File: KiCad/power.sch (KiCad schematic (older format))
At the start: 16 parts

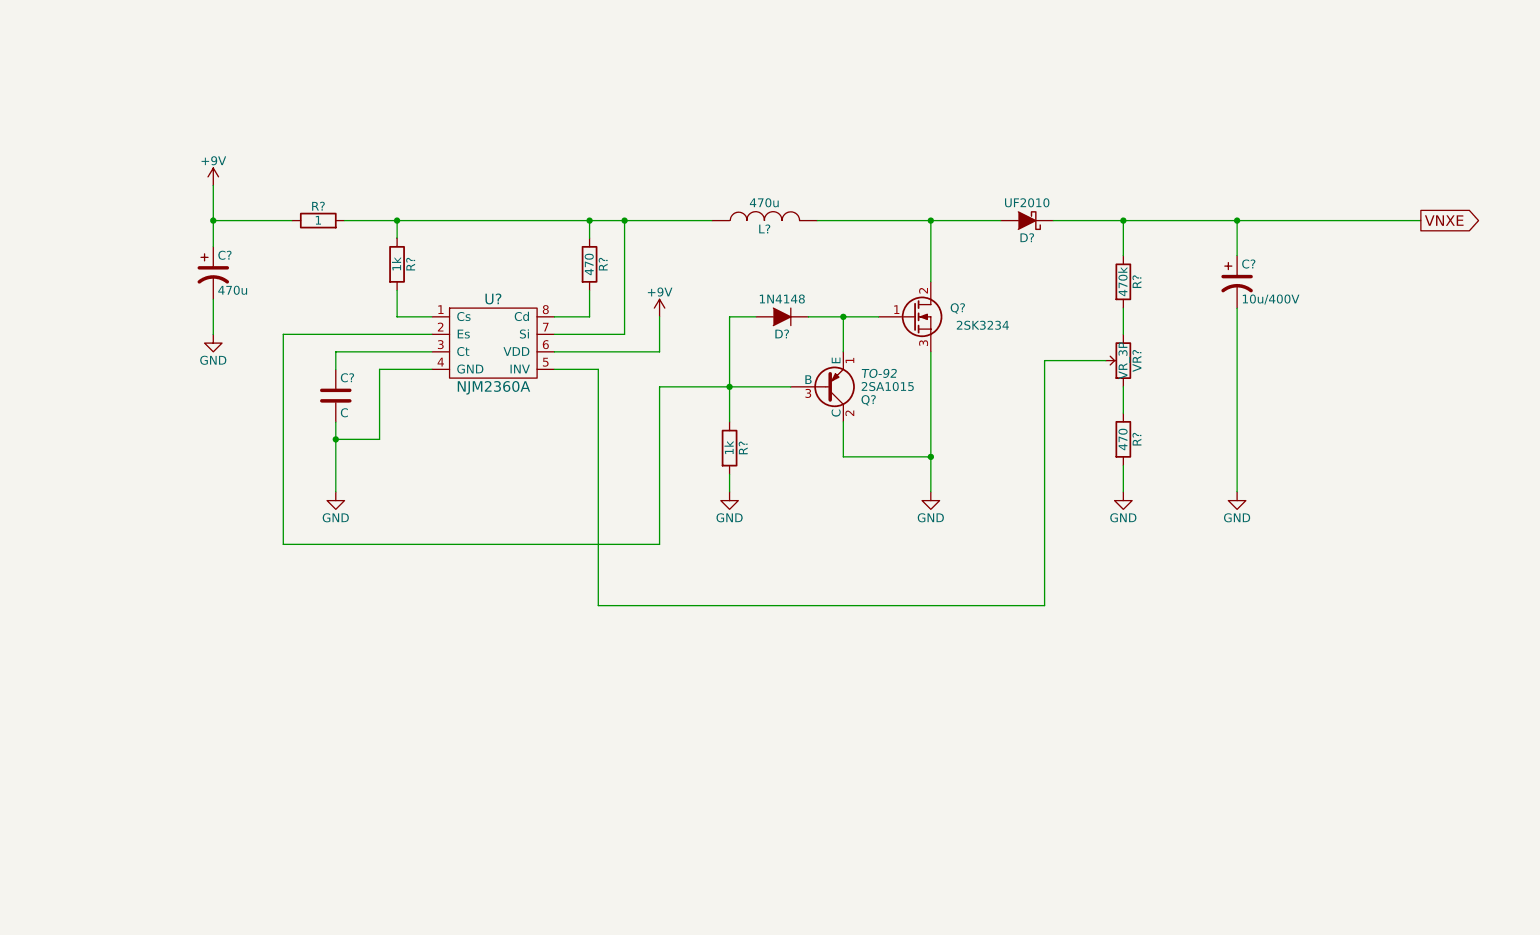
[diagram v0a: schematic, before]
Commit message: add power schematic
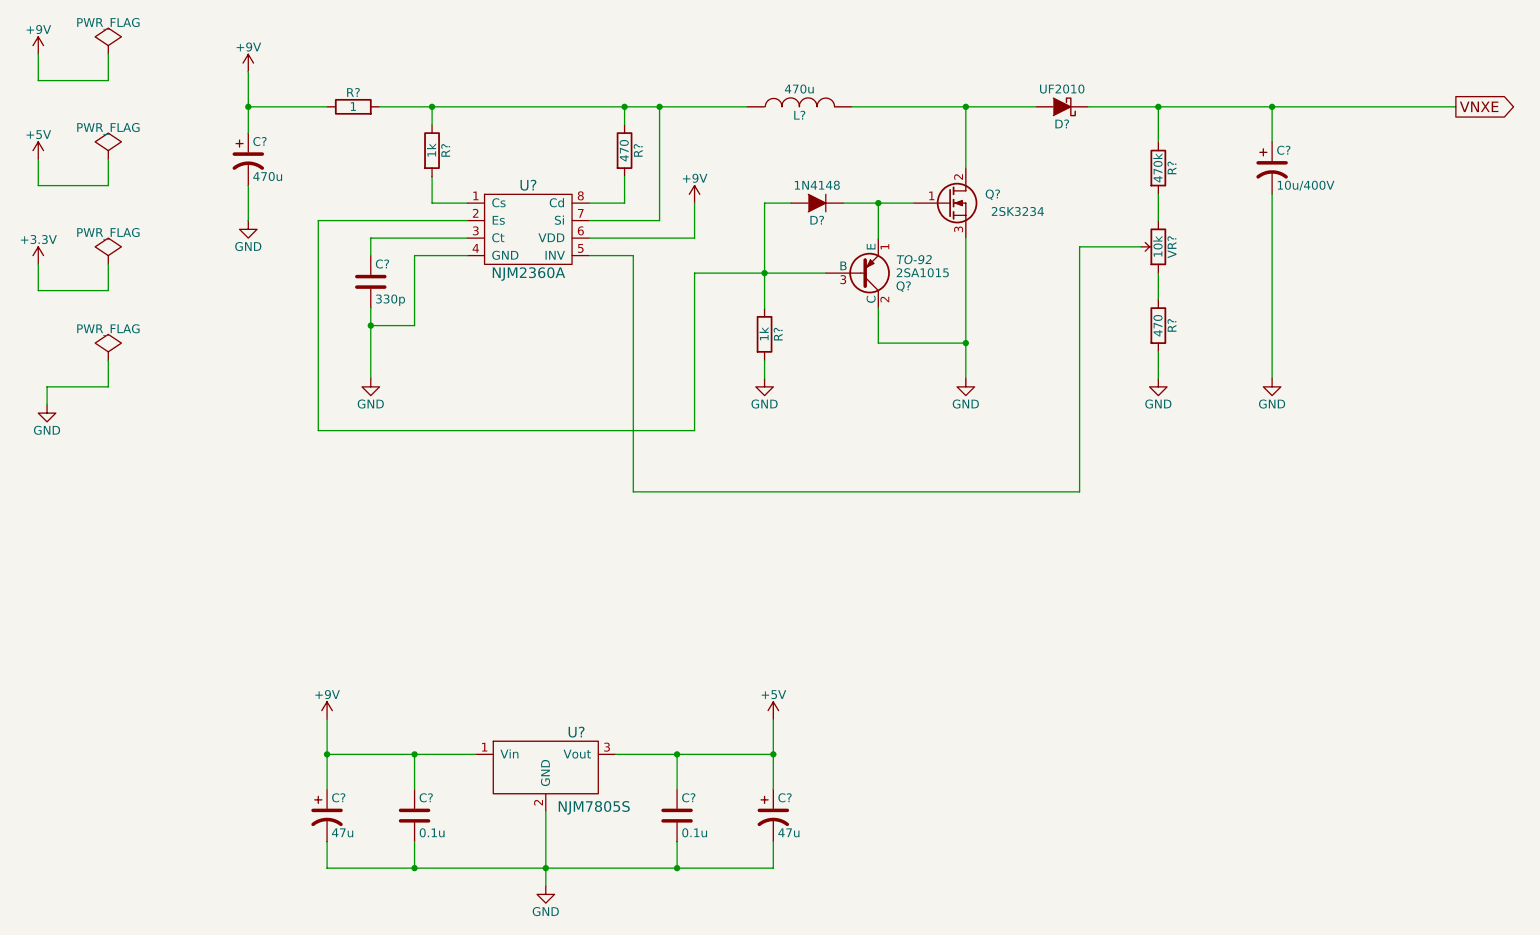
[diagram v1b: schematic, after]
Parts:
- added C? (x2): 0.1u, symbol C
- added C? (x2): 47u, symbol CP1
- added U?: NJM7805S, symbol NJM7805S
- C?: value C -> 330p
- VR?: value VR_3P -> 10k
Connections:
- net +9V: now also C?.1, C?.1, U?.1 (Vin)
- net GND: now also C?.2, C?.2, C?.2, C?.2, U?.2 (GND)
- new net +5V: C?.1, C?.1, U?.3 (Vout)
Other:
- moved on the sheet: C?, D?, L?, Q?, R?, U?, VR?

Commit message: change schematics
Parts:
- gave numbers to parts that had none: 21

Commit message: add pcb design
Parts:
- C1, C2, C6: footprint (none) -> Capacitors_ThroughHole:CP_Radial_D7.5mm_P2.50mm
- C3, C4, C5: footprint (none) -> Capacitors_ThroughHole:C_Axial_L3.8mm_D2.6mm_P7.50mm_Horizontal
- C7: footprint (none) -> Capacitors_ThroughHole:CP_Radial_D12.5mm_P5.00mm
- D1: footprint (none) -> Diodes_ThroughHole:D_A-405_P7.62mm_Horizontal
- D2: footprint (none) -> Diodes_ThroughHole:D_A-405_P10.16mm_Horizontal
- L1: footprint (none) -> Inductors_NEOSID:Neosid_Inductor_MA-Bs75
- Q1: footprint TO-92 -> TO_SOT_Packages_THT:TO-92_Inline_Wide
- Q2: footprint (none) -> TO_SOT_Packages_THT:TO-220-3_Vertical
- R10, R11, R12, R13, R8, R9: footprint (none) -> Resistors_ThroughHole:R_Axial_DIN0207_L6.3mm_D2.5mm_P10.16mm_Horizontal
- U6: footprint (none) -> Housings_DIP:DIP-8_W7.62mm
- U7: footprint (none) -> TO_SOT_Packages_SMD:TO-252-3_TabPin2
- VR1: footprint (none) -> Potentiometers:Potentiometer_Triwood_RM-065
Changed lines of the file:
@@
 F 0 "U6" H 3650 2350 60  0000 C CNN
 F 1 "NJM2360A" H 3650 1850 60  0000 C CNN
-F 2 "" H 3400 2100 60  0000 C CNN
+F 2 "Housings_DIP:DIP-8_W7.62mm" H 3400 2100 60  0001 C CNN
 F 3 "" H 3400 2100 60  0000 C CNN
 	1    3650 2100
@@
 F 0 "Q1" H 5750 2425 50  0000 L CNN
 F 1 "2SA1015" H 5750 2350 50  0000 L CNN
-F 2 "TO-92" H 5750 2275 50  0000 L CIN
+F 2 "TO_SOT_Packages_THT:TO-92_Inline_Wide" H 5750 2275 50  0001 L CIN
 F 3 "" H 5550 2350 50  0000 L CNN
 	1    5550 2350
@@
 F 0 "Q2" H 6350 2000 50  0000 R CNN
 F 1 "2SK3234" H 6600 1900 50  0000 R CNN
-F 2 "" H 6250 2050 50  0000 C CNN
+F 2 "TO_SOT_Packages_THT:TO-220-3_Vertical" H 6250 2050 50  0001 C CNN
 F 3 "" H 6050 1950 50  0000 C CNN
 	1    6050 1950
@@
 F 0 "D2" H 6700 1500 50  0000 C CNN
 F 1 "UF2010" H 6700 1300 50  0000 C CNN
-F 2 "" H 6700 1400 50  0000 C CNN
+F 2 "Diodes_ThroughHole:D_A-405_P10.16mm_Horizontal" H 6700 1400 50  0001 C CNN
 F 3 "" H 6700 1400 50  0000 C CNN
 	1    6700 1400
@@
 F 0 "D1" H 5300 2050 50  0000 C CNN
 F 1 "1N4148" H 5300 1850 50  0000 C CNN
-F 2 "" H 5300 1950 50  0000 C CNN
+F 2 "Diodes_ThroughHole:D_A-405_P7.62mm_Horizontal" H 5300 1950 50  0001 C CNN
 F 3 "" H 5300 1950 50  0000 C CNN
 	1    5300 1950
@@
 F 0 "R11" V 5080 2700 50  0000 C CNN
 F 1 "1k" V 5000 2700 50  0000 C CNN
-F 2 "" V 4930 2700 50  0000 C CNN
+F 2 "Resistors_ThroughHole:R_Axial_DIN0207_L6.3mm_D2.5mm_P10.16mm_Horizontal" V 4930 2700 50  0001 C CNN
 F 3 "" H 5000 2700 50  0000 C CNN
 	1    5000 2700
@@
 F 0 "R10" V 4280 1650 50  0000 C CNN
 F 1 "470" V 4200 1650 50  0000 C CNN
-F 2 "" V 4130 1650 50  0000 C CNN
+F 2 "Resistors_ThroughHole:R_Axial_DIN0207_L6.3mm_D2.5mm_P10.16mm_Horizontal" V 4130 1650 50  0001 C CNN
 F 3 "" H 4200 1650 50  0000 C CNN
 	1    4200 1650
@@
 F 0 "R9" V 3180 1650 50  0000 C CNN
 F 1 "1k" V 3100 1650 50  0000 C CNN
-F 2 "" V 3030 1650 50  0000 C CNN
+F 2 "Resistors_ThroughHole:R_Axial_DIN0207_L6.3mm_D2.5mm_P10.16mm_Horizontal" V 3030 1650 50  0001 C CNN
 F 3 "" H 3100 1650 50  0000 C CNN
 	1    3100 1650
@@
 F 0 "R8" V 2730 1400 50  0000 C CNN
 F 1 "1" V 2650 1400 50  0000 C CNN
-F 2 "" V 2580 1400 50  0000 C CNN
+F 2 "Resistors_ThroughHole:R_Axial_DIN0207_L6.3mm_D2.5mm_P10.16mm_Horizontal" V 2580 1400 50  0001 C CNN
 F 3 "" H 2650 1400 50  0000 C CNN
 	1    2650 1400
@@
 F 0 "R12" V 7330 1750 50  0000 C CNN
 F 1 "470k" V 7250 1750 50  0000 C CNN
-F 2 "" V 7180 1750 50  0000 C CNN
+F 2 "Resistors_ThroughHole:R_Axial_DIN0207_L6.3mm_D2.5mm_P10.16mm_Horizontal" V 7180 1750 50  0001 C CNN
 F 3 "" H 7250 1750 50  0000 C CNN
 	1    7250 1750
@@
 F 0 "C3" H 2775 2500 50  0000 L CNN
 F 1 "330p" H 2775 2300 50  0000 L CNN
-F 2 "" H 2788 2250 50  0000 C CNN
+F 2 "Capacitors_ThroughHole:C_Axial_L3.8mm_D2.6mm_P7.50mm_Horizontal" H 2788 2250 50  0001 C CNN
 F 3 "" H 2750 2400 50  0000 C CNN
 	1    2750 2400
@@
 F 0 "C1" H 2075 1800 50  0000 L CNN
 F 1 "470u" H 2075 1600 50  0000 L CNN
-F 2 "" H 2050 1700 50  0000 C CNN
+F 2 "Capacitors_ThroughHole:CP_Radial_D7.5mm_P2.50mm" H 2050 1700 50  0001 C CNN
 F 3 "" H 2050 1700 50  0000 C CNN
 	1    2050 1700
@@
 F 0 "C7" H 7925 1850 50  0000 L CNN
 F 1 "10u/400V" H 7925 1650 50  0000 L CNN
-F 2 "" H 7900 1750 50  0000 C CNN
+F 2 "Capacitors_ThroughHole:CP_Radial_D12.5mm_P5.00mm" H 7900 1750 50  0001 C CNN
 F 3 "" H 7900 1750 50  0000 C CNN
 	1    7900 1750
@@
 F 0 "L1" V 5150 1400 50  0000 C CNN
 F 1 "470u" V 5300 1400 50  0000 C CNN
-F 2 "" H 5200 1400 50  0000 C CNN
+F 2 "Inductors_NEOSID:Neosid_Inductor_MA-Bs75" H 5200 1400 50  0001 C CNN
 F 3 "" H 5200 1400 50  0000 C CNN
 	1    5200 1400
@@
 F 0 "R13" V 7330 2650 50  0000 C CNN
 F 1 "470" V 7250 2650 50  0000 C CNN
-F 2 "" V 7180 2650 50  0000 C CNN
+F 2 "Resistors_ThroughHole:R_Axial_DIN0207_L6.3mm_D2.5mm_P10.16mm_Horizontal" V 7180 2650 50  0001 C CNN
 F 3 "" H 7250 2650 50  0000 C CNN
 	1    7250 2650
@@
 F 0 "VR1" V 7330 2200 50  0000 C CNN
 F 1 "10k" V 7250 2200 50  0000 C CNN
-F 2 "" V 7180 2200 50  0000 C CNN
+F 2 "Potentiometers:Potentiometer_Triwood_RM-065" V 7180 2200 50  0001 C CNN
 F 3 "" H 7250 2200 50  0000 C CNN
 	1    7250 2200
@@
 F 0 "U7" H 3925 5225 60  0000 C CNN
 F 1 "NJM7805S" H 4025 4800 60  0000 C CNN
-F 2 "" H 3650 5100 60  0000 C CNN
+F 2 "TO_SOT_Packages_SMD:TO-252-3_TabPin2" H 3650 5100 60  0001 C CNN
 F 3 "" H 3650 5100 60  0000 C CNN
 	1    3650 5100
@@
 F 0 "C4" H 3025 5550 50  0000 L CNN
 F 1 "0.1u" H 3025 5350 50  0000 L CNN
-F 2 "" H 3038 5300 50  0000 C CNN
+F 2 "Capacitors_ThroughHole:C_Axial_L3.8mm_D2.6mm_P7.50mm_Horizontal" H 3038 5300 50  0001 C CNN
 F 3 "" H 3000 5450 50  0000 C CNN
 	1    3000 5450
@@
 F 0 "C5" H 4525 5550 50  0000 L CNN
 F 1 "0.1u" H 4525 5350 50  0000 L CNN
-F 2 "" H 4538 5300 50  0000 C CNN
+F 2 "Capacitors_ThroughHole:C_Axial_L3.8mm_D2.6mm_P7.50mm_Horizontal" H 4538 5300 50  0001 C CNN
 F 3 "" H 4500 5450 50  0000 C CNN
 	1    4500 5450
@@
 F 0 "C2" H 2525 5550 50  0000 L CNN
 F 1 "47u" H 2525 5350 50  0000 L CNN
-F 2 "" H 2500 5450 50  0000 C CNN
+F 2 "Capacitors_ThroughHole:CP_Radial_D7.5mm_P2.50mm" H 2500 5450 50  0001 C CNN
 F 3 "" H 2500 5450 50  0000 C CNN
 	1    2500 5450
@@
 F 0 "C6" H 5075 5550 50  0000 L CNN
 F 1 "47u" H 5075 5350 50  0000 L CNN
-F 2 "" H 5050 5450 50  0000 C CNN
+F 2 "Capacitors_ThroughHole:CP_Radial_D7.5mm_P2.50mm" H 5050 5450 50  0001 C CNN
 F 3 "" H 5050 5450 50  0000 C CNN
 	1    5050 5450

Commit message: change some pcb packages
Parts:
- added CON1: BARREL_JACK, Connect:BARREL_JACK, symbol BARREL_JACK
- C3, C4, C5: footprint Capacitors_ThroughHole:C_Axial_L3.8mm_D2.6mm_P7.50mm_Horizontal -> Capacitors_SMD:C_0603
- D1: value 1N4148 -> 1N4148W; footprint Diodes_ThroughHole:D_A-405_P7.62mm_Horizontal -> Diodes_SMD:D_SOD-123
- L1: value 470u -> LHL13NB471K; footprint Inductors_NEOSID:Neosid_Inductor_MA-Bs75 -> nixie_clock:LHL13NB471K
- R10, R11, R12, R13, R9: footprint Resistors_ThroughHole:R_Axial_DIN0207_L6.3mm_D2.5mm_P10.16mm_Horizontal -> Resistors_SMD:R_1206
- R8: footprint Resistors_ThroughHole:R_Axial_DIN0207_L6.3mm_D2.5mm_P10.16mm_Horizontal -> Resistors_SMD:R_2512
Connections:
- net +9V: now also CON1.1
- net GND: now also CON1.2, CON1.3
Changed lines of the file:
@@
 P 5300 1950
 F 0 "D1" H 5300 2050 50  0000 C CNN
-F 1 "1N4148" H 5300 1850 50  0000 C CNN
-F 2 "Diodes_ThroughHole:D_A-405_P7.62mm_Horizontal" H 5300 1950 50  0001 C CNN
+F 1 "1N4148W" H 5300 1850 50  0000 C CNN
+F 2 "Diodes_SMD:D_SOD-123" H 5300 1950 50  0001 C CNN
 F 3 "" H 5300 1950 50  0000 C CNN
 	1    5300 1950
@@
 F 0 "R11" V 5080 2700 50  0000 C CNN
 F 1 "1k" V 5000 2700 50  0000 C CNN
-F 2 "Resistors_ThroughHole:R_Axial_DIN0207_L6.3mm_D2.5mm_P10.16mm_Horizontal" V 4930 2700 50  0001 C CNN
+F 2 "Resistors_SMD:R_1206" V 4930 2700 50  0001 C CNN
 F 3 "" H 5000 2700 50  0000 C CNN
 	1    5000 2700
@@
 F 0 "R10" V 4280 1650 50  0000 C CNN
 F 1 "470" V 4200 1650 50  0000 C CNN
-F 2 "Resistors_ThroughHole:R_Axial_DIN0207_L6.3mm_D2.5mm_P10.16mm_Horizontal" V 4130 1650 50  0001 C CNN
+F 2 "Resistors_SMD:R_1206" V 4130 1650 50  0001 C CNN
 F 3 "" H 4200 1650 50  0000 C CNN
 	1    4200 1650
@@
 F 0 "R9" V 3180 1650 50  0000 C CNN
 F 1 "1k" V 3100 1650 50  0000 C CNN
-F 2 "Resistors_ThroughHole:R_Axial_DIN0207_L6.3mm_D2.5mm_P10.16mm_Horizontal" V 3030 1650 50  0001 C CNN
+F 2 "Resistors_SMD:R_1206" V 3030 1650 50  0001 C CNN
 F 3 "" H 3100 1650 50  0000 C CNN
 	1    3100 1650
@@
 F 0 "R8" V 2730 1400 50  0000 C CNN
 F 1 "1" V 2650 1400 50  0000 C CNN
-F 2 "Resistors_ThroughHole:R_Axial_DIN0207_L6.3mm_D2.5mm_P10.16mm_Horizontal" V 2580 1400 50  0001 C CNN
+F 2 "Resistors_SMD:R_2512" V 2580 1400 50  0001 C CNN
 F 3 "" H 2650 1400 50  0000 C CNN
 	1    2650 1400
@@
 F 0 "R12" V 7330 1750 50  0000 C CNN
 F 1 "470k" V 7250 1750 50  0000 C CNN
-F 2 "Resistors_ThroughHole:R_Axial_DIN0207_L6.3mm_D2.5mm_P10.16mm_Horizontal" V 7180 1750 50  0001 C CNN
+F 2 "Resistors_SMD:R_1206" V 7180 1750 50  0001 C CNN
 F 3 "" H 7250 1750 50  0000 C CNN
 	1    7250 1750
@@
 F 0 "C3" H 2775 2500 50  0000 L CNN
 F 1 "330p" H 2775 2300 50  0000 L CNN
-F 2 "Capacitors_ThroughHole:C_Axial_L3.8mm_D2.6mm_P7.50mm_Horizontal" H 2788 2250 50  0001 C CNN
+F 2 "Capacitors_SMD:C_0603" H 2788 2250 50  0001 C CNN
 F 3 "" H 2750 2400 50  0000 C CNN
 	1    2750 2400
@@
 P 5200 1400
 F 0 "L1" V 5150 1400 50  0000 C CNN
-F 1 "470u" V 5300 1400 50  0000 C CNN
-F 2 "Inductors_NEOSID:Neosid_Inductor_MA-Bs75" H 5200 1400 50  0001 C CNN
+F 1 "LHL13NB471K" V 5300 1400 50  0000 C CNN
+F 2 "nixie_clock:LHL13NB471K" H 5200 1400 50  0001 C CNN
 F 3 "" H 5200 1400 50  0000 C CNN
 	1    5200 1400
@@
 F 0 "R13" V 7330 2650 50  0000 C CNN
 F 1 "470" V 7250 2650 50  0000 C CNN
-F 2 "Resistors_ThroughHole:R_Axial_DIN0207_L6.3mm_D2.5mm_P10.16mm_Horizontal" V 7180 2650 50  0001 C CNN
+F 2 "Resistors_SMD:R_1206" V 7180 2650 50  0001 C CNN
 F 3 "" H 7250 2650 50  0000 C CNN
 	1    7250 2650
@@
 F 0 "C4" H 3025 5550 50  0000 L CNN
 F 1 "0.1u" H 3025 5350 50  0000 L CNN
-F 2 "Capacitors_ThroughHole:C_Axial_L3.8mm_D2.6mm_P7.50mm_Horizontal" H 3038 5300 50  0001 C CNN
+F 2 "Capacitors_SMD:C_0603" H 3038 5300 50  0001 C CNN
 F 3 "" H 3000 5450 50  0000 C CNN
 	1    3000 5450
@@
 F 0 "C5" H 4525 5550 50  0000 L CNN
 F 1 "0.1u" H 4525 5350 50  0000 L CNN
-F 2 "Capacitors_ThroughHole:C_Axial_L3.8mm_D2.6mm_P7.50mm_Horizontal" H 4538 5300 50  0001 C CNN
+F 2 "Capacitors_SMD:C_0603" H 4538 5300 50  0001 C CNN
 F 3 "" H 4500 5450 50  0000 C CNN
 	1    4500 5450
@@
 Wire Wire Line
 	1250 1750 1250 1600
+$Comp
+L BARREL_JACK CON1
+U 1 1 59EA9744
+P 1300 4000
+F 0 "CON1" H 1300 4250 50  0000 C CNN
+F 1 "BARREL_JACK" H 1300 3800 50  0000 C CNN
+F 2 "Connect:BARREL_JACK" H 1300 4000 50  0001 C CNN
+F 3 "" H 1300 4000 50  0000 C CNN
+	1    1300 4000
+	1    0    0    -1
+$EndComp
+Wire Wire Line
+	1600 3900 1850 3900
+Wire Wire Line
+	1850 3900 1850 3600
+Wire Wire Line
+	1600 4000 1850 4000
+Wire Wire Line
+	1850 4000 1850 4300
+Wire Wire Line
+	1600 4100 1850 4100
+Connection ~ 1850 4100
+$Comp
+L GND #PWR029
+U 1 1 59EA9E83
+P 1850 4300
+F 0 "#PWR029" H 1850 4050 50  0001 C CNN
+F 1 "GND" H 1850 4150 50  0000 C CNN
+F 2 "" H 1850 4300 50  0000 C CNN
+F 3 "" H 1850 4300 50  0000 C CNN
+	1    1850 4300
+	1    0    0    -1
+$EndComp
+$Comp
+L +9V #PWR030
+U 1 1 59EAA3F3
+P 1850 3600
+F 0 "#PWR030" H 1850 3450 50  0001 C CNN
+F 1 "+9V" H 1850 3740 50  0000 C CNN
+F 2 "" H 1850 3600 50  0000 C CNN
+F 3 "" H 1850 3600 50  0000 C CNN
+	1    1850 3600
+	1    0    0    -1
+$EndComp
 $EndSCHEMATC
